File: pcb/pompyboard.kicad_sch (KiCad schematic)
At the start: 0 parts

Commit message: pcb: initial commit
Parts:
- added C229: 10u, Capacitor_SMD:C_0201_0603Metric, symbol Device:C
- added C230, C232: 0.1u, Capacitor_SMD:C_0201_0603Metric, symbol Device:C
- added C231: 100u, Capacitor_SMD:C_0201_0603Metric, symbol Device:C
- added D1: F.0603.00139/P2-0603R1TS2-06T-002, LED_SMD:LED_0201_0603Metric, symbol Device:LED
- added J1: USB_C_Receptacle_USB2.0_16P, Connector_USB:USB_C_Receptacle_GCT_USB4085, symbol Connector:USB_C_Receptacle_USB2.0_16P
- added J2: Conn_01x04_Pin, Connector_PinHeader_1.00mm:PinHeader_1x04_P1.00mm_Horizontal, symbol Connector:Conn_01x04_Pin
- added R210, R211: 5.1k, Resistor_SMD:R_0201_0603Metric, symbol Device:R
- added R212: 1k, Resistor_SMD:R_0201_0603Metric, symbol Device:R
- added R213: 10k, Resistor_SMD:R_0201_0603Metric, symbol Device:R
- added SW1: EVQQ2B03W, Button_Switch_SMD:SW_SPST_EVQQ2, symbol Switch:SW_Push
- added U229: STM32F429IGTx, Package_QFP:LQFP-176_24x24mm_P0.5mm, symbol MCU_ST_STM32F4:STM32F429IGTx
- added U230: USB3320C-EZK-TR, Package_DFN_QFN:QFN-32-1EP_5x5mm_P0.5mm_EP3.45x3.45mm, symbol Interface_USB:USB3300-EZK
- added U231: AMS1117CD-3.3, Package_TO_SOT_SMD:TO-252-3_TabPin2, symbol Regulator_Linear:AMS1117CD-3.3
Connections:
- new net: R213.2, SW1.1, U229.1 (PE2)
- new net: J1.A5 (CC1), R211.2
- new net: D1.2 (A), R212.2
- new net: J1.B5 (CC2), R210.1
- new net: J2.1 (Pin_1), U229.137 (PA14)
- new net: J2.2 (Pin_2), U229.124 (PA13)
- new net 3.3V: C231.1, C232.1, J2.4 (Pin_4), R213.1, U229.103 (VDD), U229.114 (VDD), U229.127 (VDD), U229.136 (VDD), U229.149 (VDD), U229.15 (VDD), U229.159 (VDD), U229.172 (VDD), U229.23 (VDD), U229.36 (VDD), U229.39 (VDDA), U229.49 (VDD), U229.62 (VDD), U229.72 (VDD), U229.82 (VDD), U229.91 (VDD), U231.2 (VO)
- new net D+: J1.A6 (D+), J1.B6 (D+), U230.7 (DP)
- new net D-: J1.A7 (D-), J1.B7 (D-), U230.8 (DM)
- new net GND: C229.2, C230.2, C231.2, C232.2, D1.1 (K), J1.A1 (GND), J1.A12 (GND), J1.B1 (GND), J1.B12 (GND), J1.S1 (SHIELD), J2.3 (Pin_3), R210.2, R211.1, SW1.2, U229.102 (VSS), U229.113 (VSS), U229.126 (VSS), U229.135 (VSS), U229.14 (VSS), U229.148 (VSS), U229.158 (VSS), U229.22 (VSS), U229.37 (VSSA), U229.61 (VSS), U229.71 (VSS), U229.90 (VSS), U230.1 (GND), U230.2 (GND), U230.33 (GND), U231.1 (GND)
- new net MCO: U229.118 (PC9), U230.28 (XI)
- new net MUX0_OUT: U229.19 (PF3)
- new net MUX10_OUT: U229.35 (PC3)
- new net MUX11_OUT: U229.41 (PA1)
- new net MUX12_OUT: U229.42 (PA2)
- new net MUX13_OUT: U229.47 (PA3)
- new net MUX14_OUT: U229.50 (PA4)
- new net MUX15_OUT: U229.52 (PA6)
- new net MUX16_OUT: U229.53 (PA7)
- new net MUX17_OUT: U229.54 (PC4)
- new net MUX18_OUT: U229.55 (PC5)
- new net MUX1_OUT: U229.20 (PF4)
- new net MUX2_OUT: U229.21 (PF5)
- new net MUX3_OUT: U229.24 (PF6)
- new net MUX4_OUT: U229.25 (PF7)
- new net MUX5_OUT: U229.26 (PF8)
- new net MUX6_OUT: U229.27 (PF9)
- new net MUX7_OUT: U229.28 (PF10)
- new net MUX8_OUT: U229.33 (PC1)
- new net MUX9_OUT: U229.34 (PC2)
- new net S0: U229.5 (PE6)
- new net S1: U229.4 (PE5)
- new net S2: U229.3 (PE4)
- new net S3: U229.2 (PE3)
- new net ULPI_CK: U229.51 (PA5), U230.14 (CLKOUT)
- new net ULPI_D0: U229.44 (PH3), U230.24 (DATA0)
- new net ULPI_D1: U229.56 (PB0), U230.23 (DATA1)
- new net ULPI_D2: U229.57 (PB1), U230.22 (DATA2)
- new net ULPI_D3: U229.79 (PB10), U230.21 (DATA3)
- new net ULPI_D4: U229.80 (PB11), U230.20 (DATA4)
- new net ULPI_D5: U229.92 (PB12), U230.19 (DATA5)
- new net ULPI_D6: U229.93 (PB13), U230.18 (DATA6)
- new net ULPI_D7: U229.163 (PB5), U230.17 (DATA7)
- new net ULPI_DIR: U229.13 (PI11), U230.12 (DIR)
- new net ULPI_NXT: U229.45 (PH4), U230.11 (NXT)
- new net ULPI_STP: U229.32 (PC0), U230.13 (STP)
- new net VI: C229.1, C230.1, J1.A4 (VBUS), J1.A9 (VBUS), J1.B4 (VBUS), J1.B9 (VBUS), R212.1, U230.4 (VBUS), U231.3 (VI)
- no-connect marks 0 -> 125
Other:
- added sheet sensor column0 (sensor_column.kicad_sch)
- added sheet sensor column1 (sensor_column.kicad_sch)
- added sheet sensor column10 (sensor_column.kicad_sch)
- added sheet sensor column11 (sensor_column.kicad_sch)
- added sheet sensor column12 (sensor_column.kicad_sch)
- added sheet sensor column13 (sensor_column.kicad_sch)
- added sheet sensor column14 (sensor_column.kicad_sch)
- added sheet sensor column15 (sensor_column.kicad_sch)
- added sheet sensor column16 (sensor_column.kicad_sch)
- added sheet sensor column17 (sensor_column.kicad_sch)
- added sheet sensor column18 (sensor_column.kicad_sch)
- added sheet sensor column2 (sensor_column.kicad_sch)
- added sheet sensor column3 (sensor_column.kicad_sch)
- added sheet sensor column4 (sensor_column.kicad_sch)
- added sheet sensor column5 (sensor_column.kicad_sch)
- added sheet sensor column6 (sensor_column.kicad_sch)
- added sheet sensor column7 (sensor_column.kicad_sch)
- added sheet sensor column8 (sensor_column.kicad_sch)
- added sheet sensor column9 (sensor_column.kicad_sch)
- note added: "19x11 Hall effect sensor array"
- note added: "ADC123_IN1"
- note added: "ADC123_IN11"
- note added: "ADC123_IN2"
- note added: "ADC123_IN3"
- note added: "ADC12_IN14"
- note added: "ADC12_IN15"
- note added: "ADC12_IN4"
- note added: "ADC12_IN6"
- note added: "ADC12_IN7"
- note added: "ADC3_IN14"
- note added: "ADC3_IN15"
- note added: "ADC3_IN4"
- note added: "ADC3_IN5"
- note added: "ADC3_IN6"
- note added: "ADC3_IN7"
- note added: "ADC3_IN8"
- note added: "ADC3_IN9"
- note added: "Button for mouse click"
- note added: "JTCK-SWCLK"
- note added: "JTMS-SWDIO"
- note added: "MCO1"
- note added: "MCO2"
- note added: "OSC_IN"
- note added: "OTG_HS_ULPI_CK/ADC12_IN5"
- note added: "OTG_HS_ULPI_D0"
- note added: "OTG_HS_ULPI_D1/ADC12_IN8"
- note added: "OTG_HS_ULPI_D2/ADC12_IN9"
- note added: "OTG_HS_ULPI_D3"
- note added: "OTG_HS_ULPI_D4"
- note added: "OTG_HS_ULPI_D5"
- note added: "OTG_HS_ULPI_D6"
- note added: "OTG_HS_ULPI_D7"
- note added: "OTG_HS_ULPI_DIR"
- note added: "OTG_HS_ULPI_DIR/ADC123_IN12"
- note added: "OTG_HS_ULPI_NXT"
- note added: "OTG_HS_ULPI_NXT/ADC123_IN13"
- note added: "OTG_HS_ULPI_STP/ADC123_IN10"
- note added: "ST Link connection for flashing firmware"
- note added: "See https://jlcpcb.com/api/file/downloadByFileSystemAccessId/8586176342744576000 Appendix A.2 (page 98) See https://ww1.microchip.com/downloads/en/AppNotes/en562704.pdf"
- note added: "See https://jlcpcb.com/api/file/downloadByFileSystemAccessId/8588905505490145280 APPLICATION HINTS (Page 4)"
- note added: "USB port & transceiver"
- note added: "Voltage Regulator"

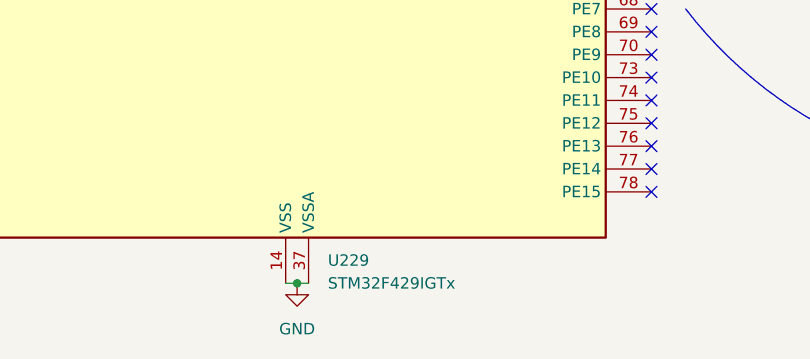
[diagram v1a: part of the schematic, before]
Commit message: pcb: select specific microcontroller (STM32F429IGTx -> STM32F429IGT6)
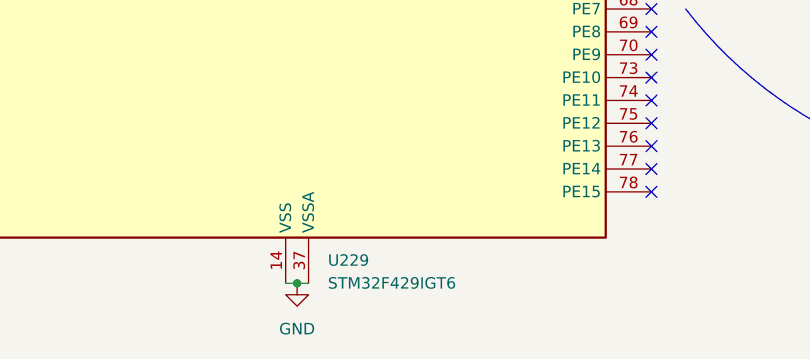
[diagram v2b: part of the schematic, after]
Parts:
- U229: value STM32F429IGTx -> STM32F429IGT6
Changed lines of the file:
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@@
 			)
 		)
-		(property "Value" "STM32F429IGTx"
+		(property "Value" "STM32F429IGT6"
 			(at 73.2633 265.43 0)
 			(effects

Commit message: pcb: fix pin size being too small
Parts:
- J2: footprint Connector_PinHeader_1.00mm:PinHeader_1x04_P1.00mm_Horizontal -> Connector_PinHeader_2.54mm:PinHeader_1x04_P2.54mm_Horizontal
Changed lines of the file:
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@@
 			)
 		)
-		(property "Footprint" "Connector_PinHeader_1.00mm:PinHeader_1x04_P1.00mm_Horizontal"
+		(property "Footprint" "Connector_PinHeader_2.54mm:PinHeader_1x04_P2.54mm_Horizontal"
 			(at 137.16 77.47 0)
 			(effects

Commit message: pcb: use capacitor footprint that actually exists for the capacity
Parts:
- C231: footprint Capacitor_SMD:C_0201_0603Metric -> Capacitor_SMD:C_1206_3216Metric
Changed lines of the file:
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@@
 			)
 		)
-		(property "Footprint" "Capacitor_SMD:C_0201_0603Metric"
+		(property "Footprint" "Capacitor_SMD:C_1206_3216Metric"
 			(at 356.5652 43.18 0)
 			(effects

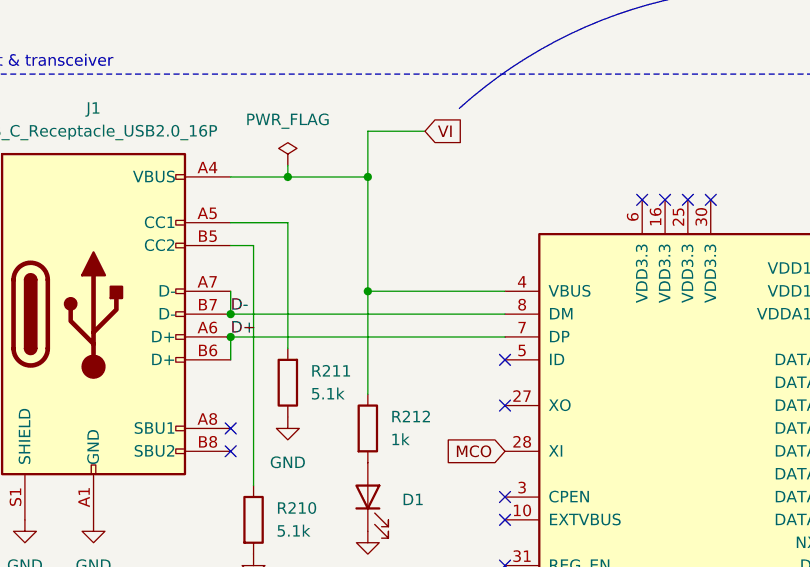
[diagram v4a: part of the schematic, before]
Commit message: pcb: add decoupling and bulk capacitor for VBUS connecting USB port and ULPI transceiver
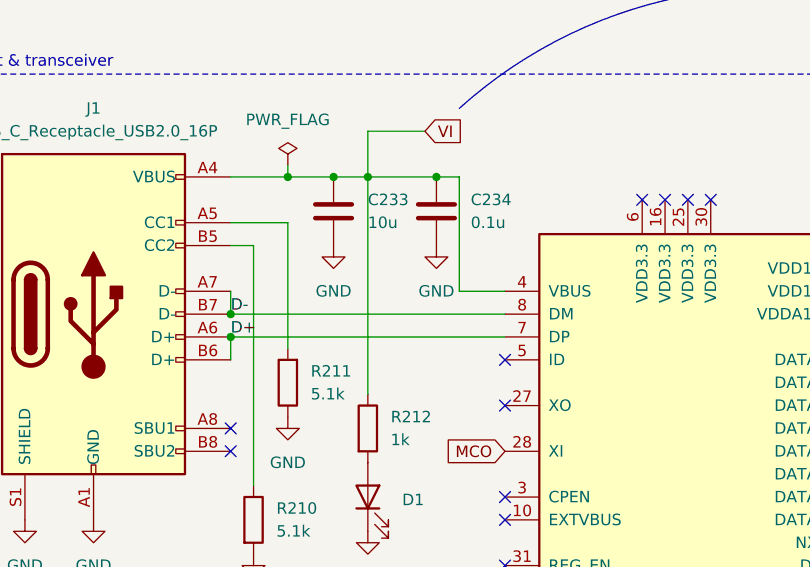
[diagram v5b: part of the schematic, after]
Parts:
- added C233: 10u, Capacitor_SMD:C_0201_0603Metric, symbol Device:C
- added C234: 0.1u, Capacitor_SMD:C_0201_0603Metric, symbol Device:C
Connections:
- net GND: now also C233.2, C234.2
- net VI: now also C233.1, C234.1

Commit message: pcb: specify component's LCSC part number
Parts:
- C229, C233: LCSC Part # (none) -> C19702
- C230, C232, C234: LCSC Part # (none) -> C1591
- C231: LCSC Part # (none) -> C6119960
- J1: LCSC Part # (none) -> C7095263
- J2: LCSC Part # (none) -> C32713263
- R210, R211: LCSC Part # (none) -> C23186
- R212: LCSC Part # (none) -> C21190
- R213: LCSC Part # (none) -> C25804
- SW1: LCSC Part # (none) -> C79178
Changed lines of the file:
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@@
+			)
+		)
+		(property "LCSC Part #" "C79178"
+			(at 137.16 222.25 0)
+			(effects
+				(font
+					(size 1.27 1.27)
+				)
+				(hide yes)
 			)
 		)
@@
 			)
 		)
+		(property "LCSC Part #" "C23186"
+			(at 217.17 59.69 0)
+			(effects
+				(font
+					(size 1.27 1.27)
+				)
+				(hide yes)
+			)
+		)
 		(pin "1"
 		)
@@
 			)
 		)
+		(property "LCSC Part #" "C25804"
+			(at 123.19 218.44 0)
+			(effects
+				(font
+					(size 1.27 1.27)
+				)
+				(hide yes)
+			)
+		)
 		(pin "1"
 		)
@@
 			)
 		)
+		(property "LCSC Part #" "C21190"
+			(at 226.06 64.77 0)
+			(effects
+				(font
+					(size 1.27 1.27)
+				)
+				(hide yes)
+			)
+		)
 		(pin "2"
 		)
@@
 			)
 		)
+		(property "LCSC Part #" "C6119960"
+			(at 355.6 39.37 0)
+			(effects
+				(font
+					(size 1.27 1.27)
+				)
+				(hide yes)
+			)
+		)
 		(pin "2"
 		)
@@
 		)
 		(property "Description" "Unpolarized capacitor"
+			(at 367.03 39.37 0)
+			(effects
+				(font
+					(size 1.27 1.27)
+				)
+				(hide yes)
+			)
+		)
+		(property "LCSC Part #" "C1591"
 			(at 367.03 39.37 0)
 			(effects
@@
 			)
 		)
+		(property "LCSC Part #" "C7095263"
+			(at 195.58 52.07 0)
+			(effects
+				(font
+					(size 1.27 1.27)
+				)
+				(hide yes)
+			)
+		)
 		(pin "A8"
 		)
@@
 			)
 		)
+		(property "LCSC Part #" "C23186"
+			(at 213.36 74.93 0)
+			(effects
+				(font
+					(size 1.27 1.27)
+				)
+				(hide yes)
+			)
+		)
 		(pin "1"
 		)
@@
 			)
 		)
+		(property "LCSC Part #" "C32713263"
+			(at 137.16 77.47 0)
+			(effects
+				(font
+					(size 1.27 1.27)
+				)
+				(hide yes)
+			)
+		)
 		(pin "2"
 		)
@@
 			)
 		)
+		(property "LCSC Part #" "C1591"
+			(at 327.66 39.37 0)
+			(effects
+				(font
+					(size 1.27 1.27)
+				)
+				(hide yes)
+			)
+		)
 		(pin "2"
 		)
@@
 			)
 		)
+		(property "LCSC Part #" "C19702"
+			(at 222.25 40.64 0)
+			(effects
+				(font
+					(size 1.27 1.27)
+				)
+				(hide yes)
+			)
+		)
 		(pin "2"
 		)
@@
 			)
 		)
+		(property "LCSC Part #" "C1591"
+			(at 233.68 40.64 0)
+			(effects
+				(font
+					(size 1.27 1.27)
+				)
+				(hide yes)
+			)
+		)
 		(pin "2"
 		)
@@
 			(at 316.23 39.37 0)
 			(effects
+				(font
+					(size 1.27 1.27)
+				)
+				(hide yes)
+			)
+		)
+		(property "LCSC Part #" "C19702"
+			(at 316.23 39.37 0)
+			(effects

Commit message: pcb: match component footprint with their actual size
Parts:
- C229, C233: footprint Capacitor_SMD:C_0201_0603Metric -> Capacitor_SMD:C_0603_1608Metric
- C230, C232, C234: LCSC Part # C1591 -> C160831
- D1: LCSC Part # (none) -> C7496820
- R210, R211: LCSC Part # C23186 -> C270344
- R212: LCSC Part # C21190 -> C270365
- R213: LCSC Part # C25804 -> C473048
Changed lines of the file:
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@@
 			)
 		)
-		(property "LCSC Part #" "C23186"
+		(property "LCSC Part #" "C270344"
 			(at 217.17 59.69 0)
 			(effects
@@
 			)
 		)
-		(property "LCSC Part #" "C25804"
+		(property "LCSC Part #" "C473048"
 			(at 123.19 218.44 0)
 			(effects
@@
 			)
 		)
-		(property "LCSC Part #" "C21190"
+		(property "LCSC Part #" "C270365"
 			(at 226.06 64.77 0)
 			(effects
@@
 			)
 		)
-		(property "LCSC Part #" "C1591"
+		(property "LCSC Part #" "C160831"
 			(at 367.03 39.37 0)
 			(effects
@@
 			)
 		)
+		(property "LCSC Part #" "C7496820"
+			(at 226.06 72.39 90)
+			(effects
+				(font
+					(size 1.27 1.27)
+				)
+				(hide yes)
+			)
+		)
 		(pin "1"
 		)
@@
 			)
 		)
-		(property "LCSC Part #" "C23186"
+		(property "LCSC Part #" "C270344"
 			(at 213.36 74.93 0)
 			(effects
@@
 			)
 		)
-		(property "LCSC Part #" "C1591"
+		(property "LCSC Part #" "C160831"
 			(at 327.66 39.37 0)
 			(effects
@@
 			)
 		)
-		(property "Footprint" "Capacitor_SMD:C_0201_0603Metric"
+		(property "Footprint" "Capacitor_SMD:C_0603_1608Metric"
 			(at 223.2152 44.45 0)
 			(effects
@@
 			)
 		)
-		(property "LCSC Part #" "C1591"
+		(property "LCSC Part #" "C160831"
 			(at 233.68 40.64 0)
 			(effects
@@
 			)
 		)
-		(property "Footprint" "Capacitor_SMD:C_0201_0603Metric"
+		(property "Footprint" "Capacitor_SMD:C_0603_1608Metric"
 			(at 317.1952 43.18 0)
 			(effects

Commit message: pcb: use cheaper hall effect sensor and remove unnecessary capacitor and resistor connected to each sensor
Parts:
- renumbered C233 to C20, C234 to C21, C229 to C22, C230 to C23, C231 to C24, C232 to C25, R213 to R1, R210 to R2, R211 to R3, R212 to R4
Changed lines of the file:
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@@
 		(dnp no)
 		(fields_autoplaced yes)
-		(property "Reference" "R211"
+		(property "Reference" "R3"
 			(at 219.71 58.4199 0)
 			(effects
@@
 			(project "pompyboard"
 				(path "/e5830f2e-b6bc-440e-bdf9-7651ab21e3a0"
-					(reference "R211")
+					(reference "R3")
 					(unit 1)
 				)
@@
 		(dnp no)
 		(fields_autoplaced yes)
-		(property "Reference" "R213"
+		(property "Reference" "R1"
 			(at 125.73 217.1699 0)
 			(effects
@@
 			(project ""
 				(path "/e5830f2e-b6bc-440e-bdf9-7651ab21e3a0"
-					(reference "R213")
+					(reference "R1")
 					(unit 1)
 				)
@@
 		(dnp no)
 		(fields_autoplaced yes)
-		(property "Reference" "R212"
+		(property "Reference" "R4"
 			(at 228.6 63.4999 0)
 			(effects
@@
 			(project ""
 				(path "/e5830f2e-b6bc-440e-bdf9-7651ab21e3a0"
-					(reference "R212")
+					(reference "R4")
 					(unit 1)
 				)
@@
 		(on_board yes)
 		(dnp no)
-		(property "Reference" "C231"
+		(property "Reference" "C24"
 			(at 359.41 38.0999 0)
 			(effects
@@
 			(project ""
 				(path "/e5830f2e-b6bc-440e-bdf9-7651ab21e3a0"
-					(reference "C231")
+					(reference "C24")
 					(unit 1)
 				)
@@
 		(on_board yes)
 		(dnp no)
-		(property "Reference" "C232"
+		(property "Reference" "C25"
 			(at 370.84 38.0999 0)
 			(effects
@@
 			(project "pompyboard"
 				(path "/e5830f2e-b6bc-440e-bdf9-7651ab21e3a0"
-					(reference "C232")
+					(reference "C25")
 					(unit 1)
 				)
@@
 		(dnp no)
 		(fields_autoplaced yes)
-		(property "Reference" "R210"
+		(property "Reference" "R2"
 			(at 215.9 73.6599 0)
 			(effects
@@
 			(project ""
 				(path "/e5830f2e-b6bc-440e-bdf9-7651ab21e3a0"
-					(reference "R210")
+					(reference "R2")
 					(unit 1)
 				)
@@
 		(on_board yes)
 		(dnp no)
-		(property "Reference" "C230"
+		(property "Reference" "C23"
 			(at 331.47 38.0999 0)
 			(effects
@@
 			(project "pompyboard"
 				(path "/e5830f2e-b6bc-440e-bdf9-7651ab21e3a0"
-					(reference "C230")
+					(reference "C23")
 					(unit 1)
 				)
@@
 		(on_board yes)
 		(dnp no)
-		(property "Reference" "C233"
+		(property "Reference" "C20"
 			(at 226.06 39.3699 0)
 			(effects
@@
 			(project "pompyboard"
 				(path "/e5830f2e-b6bc-440e-bdf9-7651ab21e3a0"
-					(reference "C233")
+					(reference "C20")
 					(unit 1)
 				)
@@
 		(on_board yes)
 		(dnp no)
-		(property "Reference" "C234"
+		(property "Reference" "C21"
 			(at 237.49 39.3699 0)
 			(effects
@@
 			(project "pompyboard"
 				(path "/e5830f2e-b6bc-440e-bdf9-7651ab21e3a0"
-					(reference "C234")
+					(reference "C21")
 					(unit 1)
 				)
@@
 		(on_board yes)
 		(dnp no)
-		(property "Reference" "C229"
+		(property "Reference" "C22"
 			(at 320.04 38.0999 0)
 			(effects
@@
 			(project "pompyboard"
 				(path "/e5830f2e-b6bc-440e-bdf9-7651ab21e3a0"
-					(reference "C229")
-					(unit 1)
-				)
+					(reference "C22")
+					(unit 1)
+				)
